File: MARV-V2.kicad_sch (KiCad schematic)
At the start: 0 parts

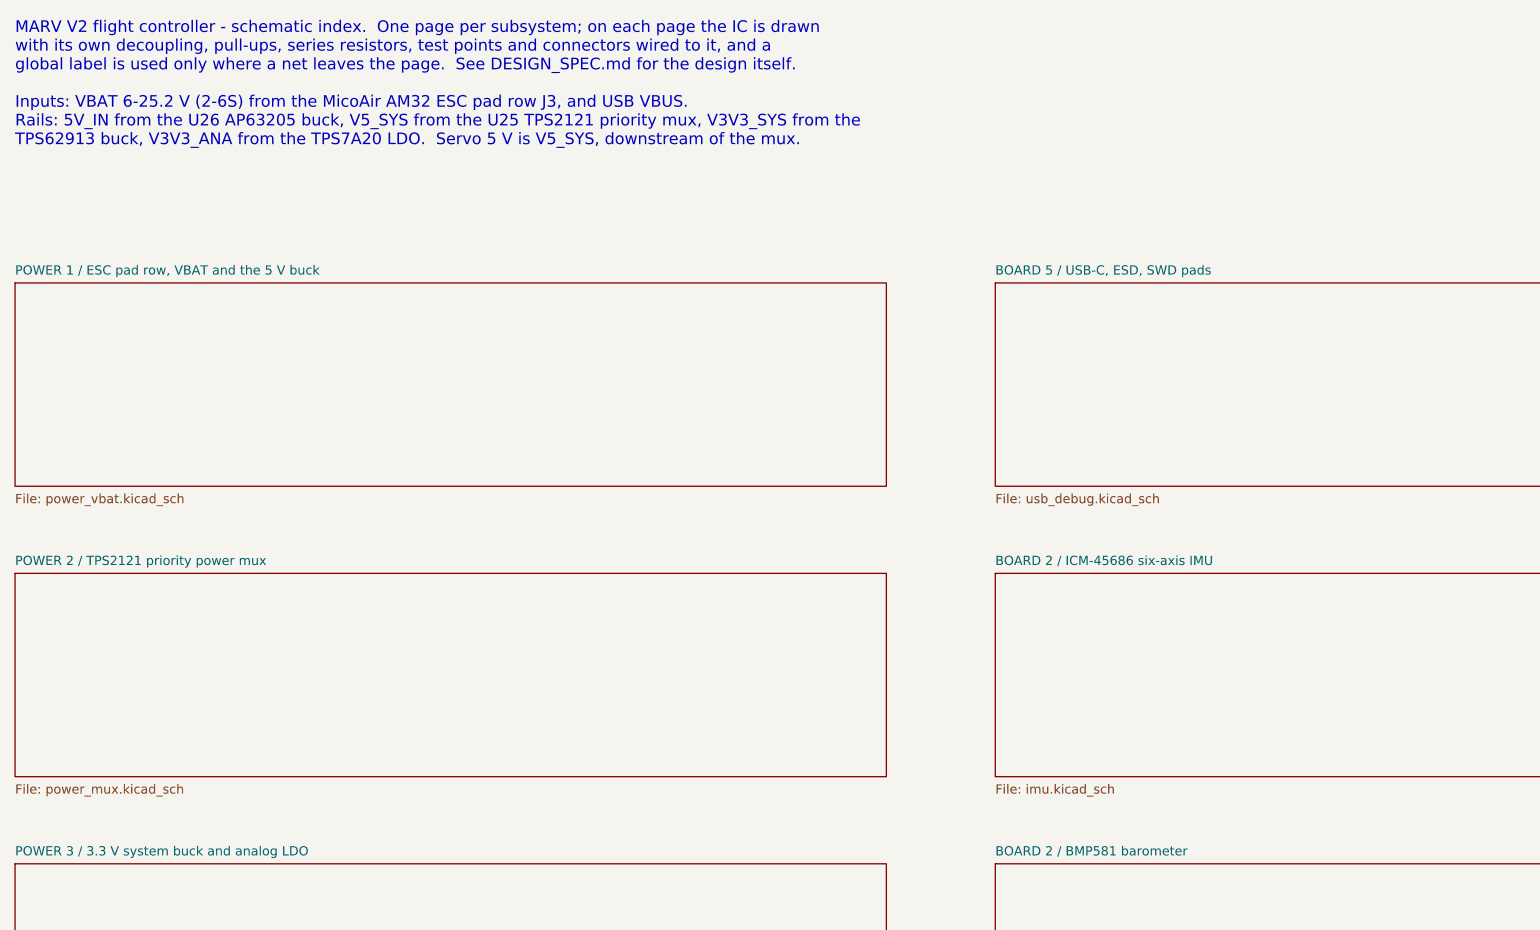
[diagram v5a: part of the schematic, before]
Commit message: Power tree: 5 V-in from an external BEC; drop pack buck, TPS2121 mux, TPS62913 stage and USB ESD
Reverses the "pack-powered from the ESC" decision, which was made without
the owner's agreement and inverted the stated requirement (5 V in from a
BEC between the ESC and the FC, so any 2-6S BEC or a 1S boost works
upstream). 140 -> 116 parts; JLC 46 -> 32 LCSC parts, 29 -> 17 Extended.

- J3 ESC row 1x08 -> 1x09: pad 7 5V_IN, pad 8 GND, pad 9 VBAT (sense only,
  feeds the R27/R28/C48 divider on GPIO41; no zone, dropped from Power class)
- USB/5V OR: Q1 AO3401A (gate on USB_VBUS, 100k pull-down) + D1 1N5819WS,
  both JLC Basic. IO-block 5 V rows, C19, C20, C21 move ahead of the FET
  onto 5V_IN; V5_SYS feeds only U7, U12 and the status LED
- 3.3 V system rail: AP63203WU-7 fixed 3.3 V buck on its datasheet
  application circuit (DS41326 Table 2; 4.7 uH FTC404030S reused per sec. 10)
  replaces TPS62913 + FB1 + 0.1 % divider + two-stage filter. JLC Basic has
  no synchronous buck at all, so this one Extended part is accepted
- U12 TPS7A2033 analog LDO kept; EN now tied to V3V3_SYS (PWR_GOOD gone)
- PWR_SRC_ST gone, GPIO37 freed (no-connect); R10 becomes the MCU_RUN pull-up
- U8 USBLC6 (Extended) removed; D+/D- straight to the 27 R series resistors
- ngspice decks that modelled the removed chain retired to
  simulations/superseded/; run_power_checks.py reports RETIRED, not PASS
- DESIGN_SPEC decisions, README, LIBRARIES, PINOUT, BOM, JLC files and
  reports regenerated

Also carries the pre-session working-tree changes (grommet footprint
MountingHole_4.0mm_Grommet -> _Pad_Via, setup_pcb floorplan, JLC tooling).

Verified: ERC 0 violations; check_power_netlist PASS (5V_IN/V5_SYS/VBAT
membership asserted); setup_pcb 0 fit/geometry problems; stitch 150 vias;
DRC 5 silk_edge_clearance warnings only (board unrouted by design);
audit_footprints 116/116; JLC live audit 0 unresolved fitted parts;
generators idempotent modulo UUIDs.

Co-Authored-By: Claude Fable 5.1 <noreply@anthrop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
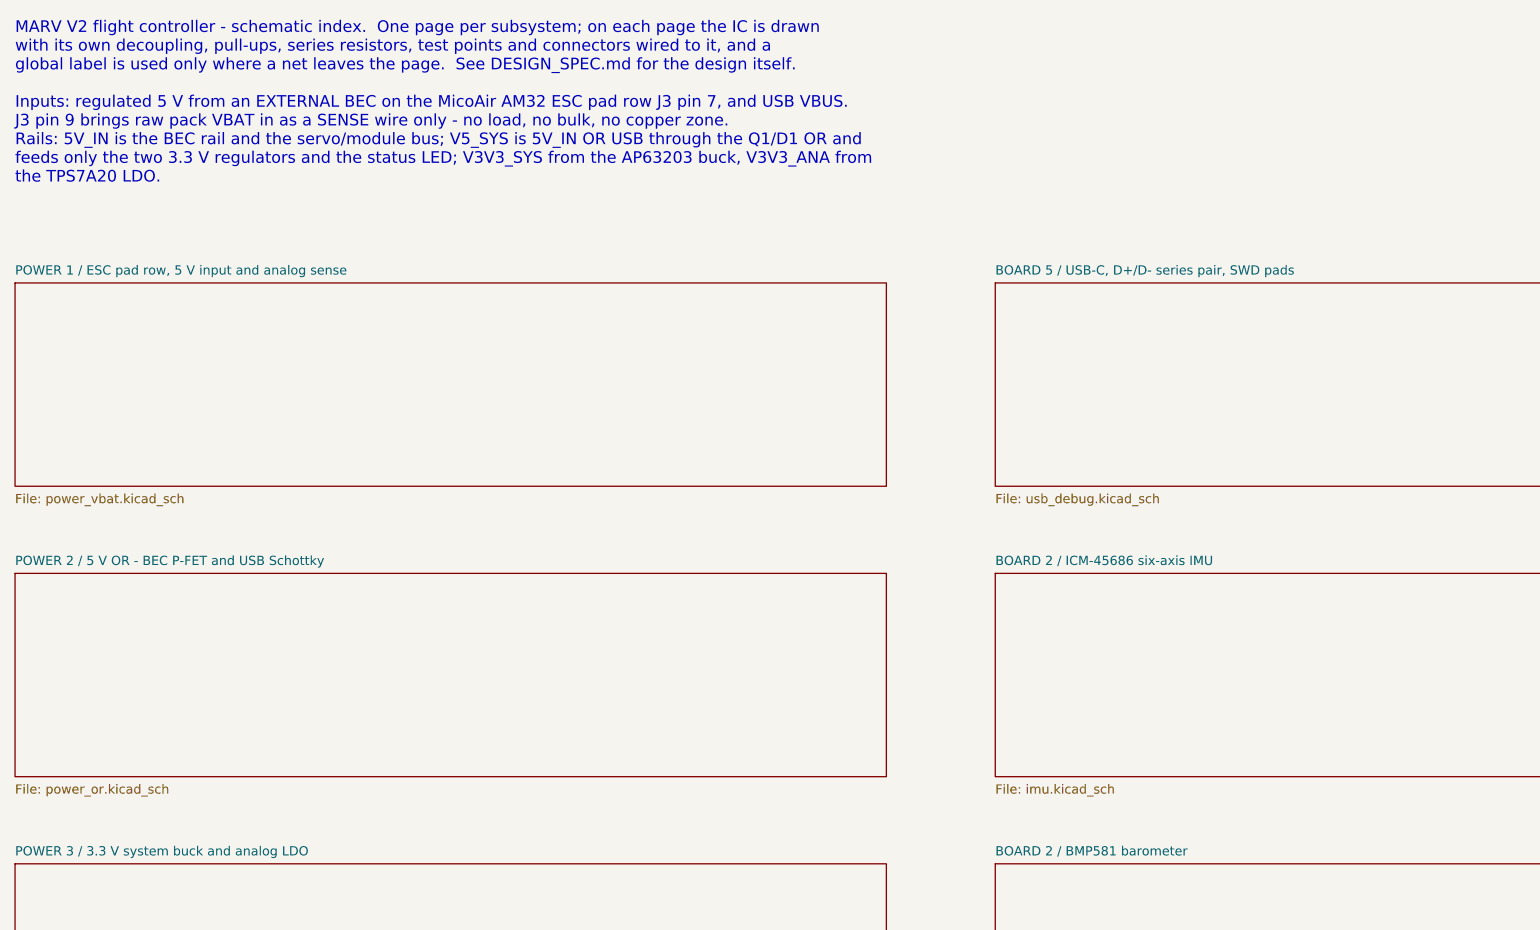
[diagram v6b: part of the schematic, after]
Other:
- sheet BOARD 5 / USB-C, ESD, SWD pads renamed BOARD 5 / USB-C, D+/D- series pair, SWD pads
- sheet POWER 1 / ESC pad row, VBAT and the 5 V buck renamed POWER 1 / ESC pad row, 5 V input and analog sense
- removed sheet POWER 2 / TPS2121 priority power mux
- added sheet POWER 2 / 5 V OR - BEC P-FET and USB Schottky (power_or.kicad_sch)
- note added: "MARV V2 flight controller - schematic index. One page per subsystem; on each page the IC is drawn with its own decoupling, pull-ups, series resistors, test points and connectors wired to it, and a global label is used only where a net leaves the page. See DESIGN_SPEC.md for the design itself. Inputs: regulated 5 V from an EXTERNAL BEC on the MicoAir AM32 ESC pad row J3 pin 7, and USB VBUS. J3 pin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"
- note removed: "MARV V2 flight controller - schematic index. One page per subsystem; on each page the IC is drawn with its own decoupling, pull-ups, series resistors, test points and connectors wired to it, and a global label is used only where a net leaves the page. See DESIGN_SPEC.md for the design itself. Inputs: VBAT 6-25.2 V (2-6S) from the MicoAir AM32 ESC pad row J3, and USB VBUS. Rails: 5V_IN from the U2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"
